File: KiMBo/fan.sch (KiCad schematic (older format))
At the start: 36 parts, among them Q14 2N7002, Q15 DMP3098L-7, Q16 2N7002, Q17 DMP3098L-7, Q18 2N7002, Q19 DMP3098L-7

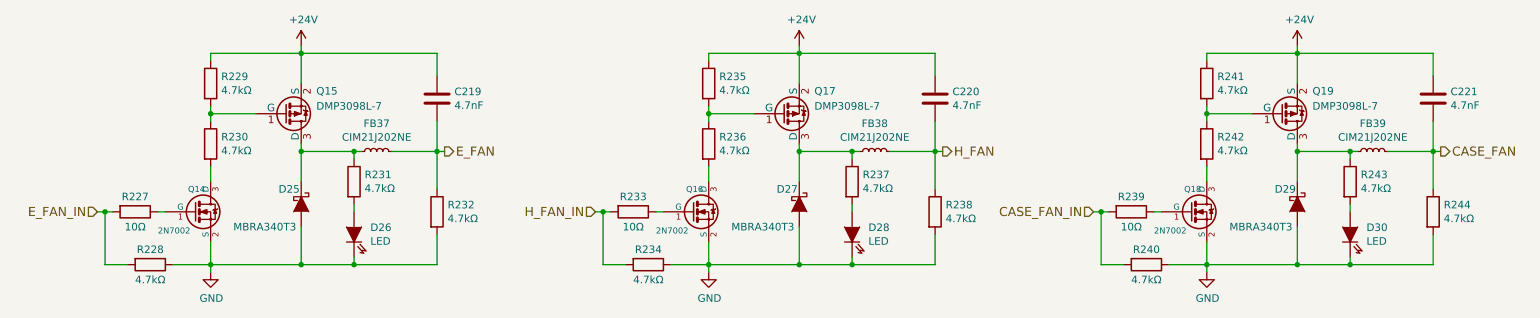
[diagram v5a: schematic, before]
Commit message: Entry of additional component values
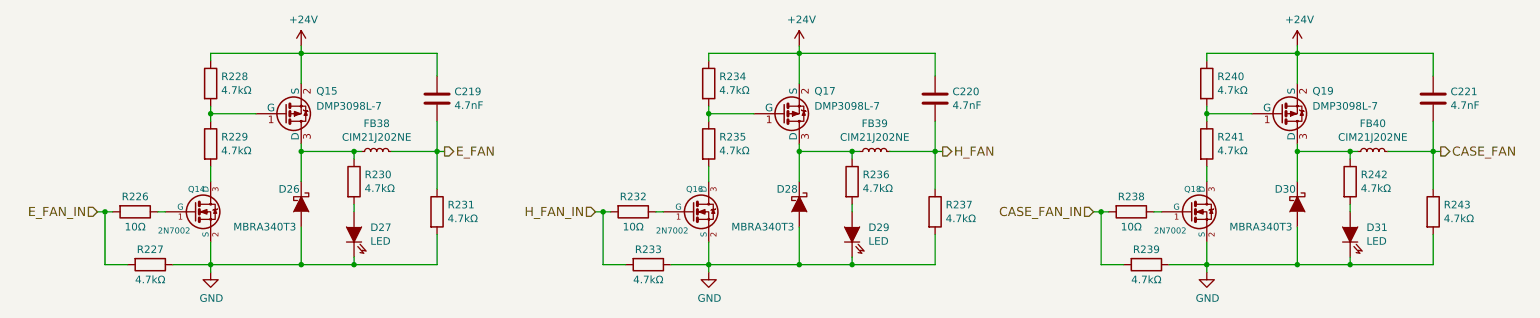
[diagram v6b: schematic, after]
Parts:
- renumbered D25 to D26, D26 to D27, D27 to D28, D28 to D29, D29 to D30, D30 to D31, FB37 to FB38, FB38 to FB39, FB39 to FB40, R227 to R226, R228 to R227, R229 to R228, R230 to R229, R231 to R230, R232 to R231, R233 to R232, R234 to R233, R235 to R234, R236 to R235, R237 to R236, R238 to R237, R239 to R238, R240 to R239, R241 to R240, R242 to R241, R243 to R242, R244 to R243
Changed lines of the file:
@@
 E_FAN
 $Comp
-L +24V #PWR0286
+L +24V #PWR0287
 U 1 1 5B5EFE55
 P 4800 4500
-F 0 "#PWR0286" H 4800 4350 50  0001 C CNN
+F 0 "#PWR0287" H 4800 4350 50  0001 C CNN
 F 1 "+24V" H 4815 4673 50  0000 C CNN
 F 2 "" H 4800 4500 50  0000 C CNN
@@
 $EndComp
 $Comp
-L GND #PWR0287
+L GND #PWR0288
 U 1 1 5B5EFE5B
 P 4200 6000
-F 0 "#PWR0287" H 4200 5750 50  0001 C CNN
+F 0 "#PWR0288" H 4200 5750 50  0001 C CNN
 F 1 "GND" H 4205 5827 50  0000 C CNN
 F 2 "" H 4200 6000 50  0000 C CNN
@@
 $EndComp
 $Comp
-L D_Schottky D25
+L D_Schottky D26
 U 1 1 5B5EFE61
 P 4800 5550
-F 0 "D25" V 4700 5400 50  0000 L CNN
+F 0 "D26" V 4700 5400 50  0000 L CNN
 F 1 "MBRA340T3" V 4950 5100 50  0000 L CNN
 F 2 "" H 4800 5550 50  0001 C CNN
@@
 $EndComp
 $Comp
-L R R227
+L R R226
 U 1 1 5B5EFE68
 P 3700 5600
-F 0 "R227" V 3600 5600 50  0000 C CNN
+F 0 "R226" V 3600 5600 50  0000 C CNN
 F 1 "10Ω" V 3800 5600 50  0000 C CNN
 F 2 "" V 3630 5600 50  0001 C CNN
@@
 $EndComp
 $Comp
-L LED_Short D26
+L LED_Short D27
 U 1 1 5B5EFE77
 P 5150 5750
-F 0 "D26" V 5196 5642 50  0000 R CNN
+F 0 "D27" V 5196 5642 50  0000 R CNN
 F 1 "LED" V 5105 5642 50  0000 R CNN
 F 2 "" H 5150 5750 50  0001 C CNN
@@
 $EndComp
 $Comp
-L R R231
+L R R230
 U 1 1 5B5EFE7E
 P 5150 5400
-F 0 "R231" H 5220 5446 50  0000 L CNN
+F 0 "R230" H 5220 5446 50  0000 L CNN
 F 1 "4.7kΩ" H 5220 5355 50  0000 L CNN
 F 2 "" V 5080 5400 50  0001 C CNN
@@
 $EndComp
 $Comp
-L R R229
+L R R228
 U 1 1 5B5EFE85
 P 4200 4750
-F 0 "R229" H 4270 4796 50  0000 L CNN
+F 0 "R228" H 4270 4796 50  0000 L CNN
 F 1 "4.7kΩ" H 4270 4705 50  0000 L CNN
 F 2 "" V 4130 4750 50  0001 C CNN
@@
 $EndComp
 $Comp
-L R R230
+L R R229
 U 1 1 5B5EFE8C
 P 4200 5150
-F 0 "R230" H 4270 5196 50  0000 L CNN
+F 0 "R229" H 4270 5196 50  0000 L CNN
 F 1 "4.7kΩ" H 4270 5105 50  0000 L CNN
 F 2 "" V 4130 5150 50  0001 C CNN
@@
 $EndComp
 $Comp
-L R R228
+L R R227
 U 1 1 5B5EFE93
 P 3800 5950
-F 0 "R228" V 3700 5950 50  0000 C CNN
+F 0 "R227" V 3700 5950 50  0000 C CNN
 F 1 "4.7kΩ" V 3900 5950 50  0000 C CNN
 F 2 "" V 3730 5950 50  0001 C CNN
@@
 $EndComp
 $Comp
-L R R232
+L R R231
 U 1 1 5B5EFE9A
 P 5700 5600
-F 0 "R232" H 5770 5646 50  0000 L CNN
+F 0 "R231" H 5770 5646 50  0000 L CNN
 F 1 "4.7kΩ" H 5770 5555 50  0000 L CNN
 F 2 "" V 5630 5600 50  0001 C CNN
@@
 $EndComp
 $Comp
-L INDUCTOR_Small FB37
+L INDUCTOR_Small FB38
 U 1 1 5B5F15E2
 P 5300 5200
-F 0 "FB37" V 5485 5200 50  0000 C CNN
+F 0 "FB38" V 5485 5200 50  0000 C CNN
 F 1 "CIM21J202NE" V 5394 5200 50  0000 C CNN
 F 2 "" H 5300 5200 50  0001 C CNN
@@
 H_FAN
 $Comp
-L +24V #PWR0288
+L +24V #PWR0289
 U 1 1 5B5F23AA
 P 8100 4500
-F 0 "#PWR0288" H 8100 4350 50  0001 C CNN
+F 0 "#PWR0289" H 8100 4350 50  0001 C CNN
 F 1 "+24V" H 8115 4673 50  0000 C CNN
 F 2 "" H 8100 4500 50  0000 C CNN
@@
 $EndComp
 $Comp
-L GND #PWR0289
+L GND #PWR0290
 U 1 1 5B5F23B0
 P 7500 6000
-F 0 "#PWR0289" H 7500 5750 50  0001 C CNN
+F 0 "#PWR0290" H 7500 5750 50  0001 C CNN
 F 1 "GND" H 7505 5827 50  0000 C CNN
 F 2 "" H 7500 6000 50  0000 C CNN
@@
 $EndComp
 $Comp
-L D_Schottky D27
+L D_Schottky D28
 U 1 1 5B5F23B6
 P 8100 5550
-F 0 "D27" V 8000 5400 50  0000 L CNN
+F 0 "D28" V 8000 5400 50  0000 L CNN
 F 1 "MBRA340T3" V 8250 5100 50  0000 L CNN
 F 2 "" H 8100 5550 50  0001 C CNN
@@
 $EndComp
 $Comp
-L R R233
+L R R232
 U 1 1 5B5F23BD
 P 7000 5600
-F 0 "R233" V 6900 5600 50  0000 C CNN
+F 0 "R232" V 6900 5600 50  0000 C CNN
 F 1 "10Ω" V 7100 5600 50  0000 C CNN
 F 2 "" V 6930 5600 50  0001 C CNN
@@
 $EndComp
 $Comp
-L LED_Short D28
+L LED_Short D29
 U 1 1 5B5F23CB
 P 8450 5750
-F 0 "D28" V 8496 5642 50  0000 R CNN
+F 0 "D29" V 8496 5642 50  0000 R CNN
 F 1 "LED" V 8405 5642 50  0000 R CNN
 F 2 "" H 8450 5750 50  0001 C CNN
@@
 $EndComp
 $Comp
-L R R237
+L R R236
 U 1 1 5B5F23D2
 P 8450 5400
-F 0 "R237" H 8520 5446 50  0000 L CNN
+F 0 "R236" H 8520 5446 50  0000 L CNN
 F 1 "4.7kΩ" H 8520 5355 50  0000 L CNN
 F 2 "" V 8380 5400 50  0001 C CNN
@@
 $EndComp
 $Comp
-L R R235
+L R R234
 U 1 1 5B5F23D9
 P 7500 4750
-F 0 "R235" H 7570 4796 50  0000 L CNN
+F 0 "R234" H 7570 4796 50  0000 L CNN
 F 1 "4.7kΩ" H 7570 4705 50  0000 L CNN
 F 2 "" V 7430 4750 50  0001 C CNN
@@
 $EndComp
 $Comp
-L R R236
+L R R235
 U 1 1 5B5F23E0
 P 7500 5150
-F 0 "R236" H 7570 5196 50  0000 L CNN
+F 0 "R235" H 7570 5196 50  0000 L CNN
 F 1 "4.7kΩ" H 7570 5105 50  0000 L CNN
 F 2 "" V 7430 5150 50  0001 C CNN
@@
 $EndComp
 $Comp
-L R R234
+L R R233
 U 1 1 5B5F23E7
 P 7100 5950
-F 0 "R234" V 7000 5950 50  0000 C CNN
+F 0 "R233" V 7000 5950 50  0000 C CNN
 F 1 "4.7kΩ" V 7200 5950 50  0000 C CNN
 F 2 "" V 7030 5950 50  0001 C CNN
@@
 $EndComp
 $Comp
-L R R238
+L R R237
 U 1 1 5B5F23EE
 P 9000 5600
-F 0 "R238" H 9070 5646 50  0000 L CNN
+F 0 "R237" H 9070 5646 50  0000 L CNN
 F 1 "4.7kΩ" H 9070 5555 50  0000 L CNN
 F 2 "" V 8930 5600 50  0001 C CNN
@@
 $EndComp
 $Comp
-L INDUCTOR_Small FB38
+L INDUCTOR_Small FB39
 U 1 1 5B5F2422
 P 8600 5200
-F 0 "FB38" V 8785 5200 50  0000 C CNN
+F 0 "FB39" V 8785 5200 50  0000 C CNN
 F 1 "CIM21J202NE" V 8694 5200 50  0000 C CNN
 F 2 "" H 8600 5200 50  0001 C CNN
@@
 CASE_FAN
 $Comp
-L +24V #PWR0290
+L +24V #PWR0291
 U 1 1 5B5F2995
 P 11400 4500
-F 0 "#PWR0290" H 11400 4350 50  0001 C CNN
+F 0 "#PWR0291" H 11400 4350 50  0001 C CNN
 F 1 "+24V" H 11415 4673 50  0000 C CNN
 F 2 "" H 11400 4500 50  0000 C CNN
@@
 $EndComp
 $Comp
-L GND #PWR0291
+L GND #PWR0292
 U 1 1 5B5F299B
 P 10800 6000
-F 0 "#PWR0291" H 10800 5750 50  0001 C CNN
+F 0 "#PWR0292" H 10800 5750 50  0001 C CNN
 F 1 "GND" H 10805 5827 50  0000 C CNN
 F 2 "" H 10800 6000 50  0000 C CNN
@@
 $EndComp
 $Comp
-L D_Schottky D29
+L D_Schottky D30
 U 1 1 5B5F29A1
 P 11400 5550
-F 0 "D29" V 11300 5400 50  0000 L CNN
+F 0 "D30" V 11300 5400 50  0000 L CNN
 F 1 "MBRA340T3" V 11550 5100 50  0000 L CNN
 F 2 "" H 11400 5550 50  0001 C CNN
@@
 $EndComp
 $Comp
-L R R239
+L R R238
 U 1 1 5B5F29A8
 P 10300 5600
-F 0 "R239" V 10200 5600 50  0000 C CNN
+F 0 "R238" V 10200 5600 50  0000 C CNN
 F 1 "10Ω" V 10400 5600 50  0000 C CNN
 F 2 "" V 10230 5600 50  0001 C CNN
@@
 $EndComp
 $Comp
-L LED_Short D30
+L LED_Short D31
 U 1 1 5B5F29B6
 P 11750 5750
-F 0 "D30" V 11796 5642 50  0000 R CNN
+F 0 "D31" V 11796 5642 50  0000 R CNN
 F 1 "LED" V 11705 5642 50  0000 R CNN
 F 2 "" H 11750 5750 50  0001 C CNN
@@
 $EndComp
 $Comp
-L R R243
+L R R242
 U 1 1 5B5F29BD
 P 11750 5400
-F 0 "R243" H 11820 5446 50  0000 L CNN
+F 0 "R242" H 11820 5446 50  0000 L CNN
 F 1 "4.7kΩ" H 11820 5355 50  0000 L CNN
 F 2 "" V 11680 5400 50  0001 C CNN
@@
 $EndComp
 $Comp
-L R R241
+L R R240
 U 1 1 5B5F29C4
 P 10800 4750
-F 0 "R241" H 10870 4796 50  0000 L CNN
+F 0 "R240" H 10870 4796 50  0000 L CNN
 F 1 "4.7kΩ" H 10870 4705 50  0000 L CNN
 F 2 "" V 10730 4750 50  0001 C CNN
@@
 $EndComp
 $Comp
-L R R242
+L R R241
 U 1 1 5B5F29CB
 P 10800 5150
-F 0 "R242" H 10870 5196 50  0000 L CNN
+F 0 "R241" H 10870 5196 50  0000 L CNN
 F 1 "4.7kΩ" H 10870 5105 50  0000 L CNN
 F 2 "" V 10730 5150 50  0001 C CNN
@@
 $EndComp
 $Comp
-L R R240
+L R R239
 U 1 1 5B5F29D2
 P 10400 5950
-F 0 "R240" V 10300 5950 50  0000 C CNN
+F 0 "R239" V 10300 5950 50  0000 C CNN
 F 1 "4.7kΩ" V 10500 5950 50  0000 C CNN
 F 2 "" V 10330 5950 50  0001 C CNN
@@
 $EndComp
 $Comp
-L R R244
+L R R243
 U 1 1 5B5F29D9
 P 12300 5600
-F 0 "R244" H 12370 5646 50  0000 L CNN
+F 0 "R243" H 12370 5646 50  0000 L CNN
 F 1 "4.7kΩ" H 12370 5555 50  0000 L CNN
 F 2 "" V 12230 5600 50  0001 C CNN
@@
 $EndComp
 $Comp
-L INDUCTOR_Small FB39
+L INDUCTOR_Small FB40
 U 1 1 5B5F2A0D
 P 11900 5200
-F 0 "FB39" V 12085 5200 50  0000 C CNN
+F 0 "FB40" V 12085 5200 50  0000 C CNN
 F 1 "CIM21J202NE" V 11994 5200 50  0000 C CNN
 F 2 "" H 11900 5200 50  0001 C CNN

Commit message: Add equivalent annotations document, associate more footprints
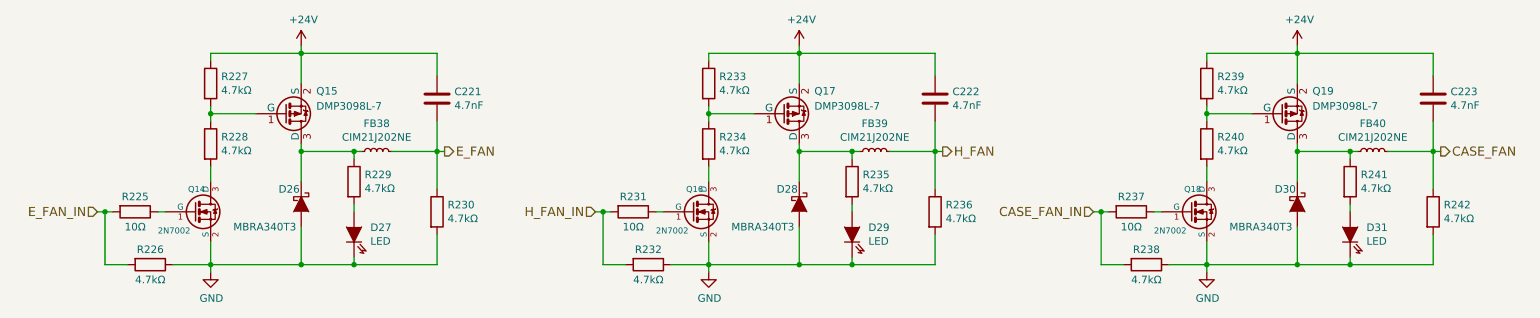
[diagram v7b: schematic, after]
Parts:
- C221: renamed from C219; footprint (none) -> Capacitors_SMD:C_0402
- C222: renamed from C220; footprint (none) -> Capacitors_SMD:C_0402
- C223: renamed from C221; footprint (none) -> Capacitors_SMD:C_0402
- renumbered R226 to R225, R227 to R226, R228 to R227, R229 to R228, R230 to R229, R231 to R230, R232 to R231, R233 to R232, R234 to R233, R235 to R234, R236 to R235, R237 to R236, R238 to R237, R239 to R238, R240 to R239, R241 to R240, R242 to R241, R243 to R242
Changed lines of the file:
@@
 E_FAN
 $Comp
-L +24V #PWR0287
+L +24V #PWR0288
 U 1 1 5B5EFE55
 P 4800 4500
-F 0 "#PWR0287" H 4800 4350 50  0001 C CNN
+F 0 "#PWR0288" H 4800 4350 50  0001 C CNN
 F 1 "+24V" H 4815 4673 50  0000 C CNN
 F 2 "" H 4800 4500 50  0000 C CNN
@@
 $EndComp
 $Comp
-L GND #PWR0288
+L GND #PWR0289
 U 1 1 5B5EFE5B
 P 4200 6000
-F 0 "#PWR0288" H 4200 5750 50  0001 C CNN
+F 0 "#PWR0289" H 4200 5750 50  0001 C CNN
 F 1 "GND" H 4205 5827 50  0000 C CNN
 F 2 "" H 4200 6000 50  0000 C CNN
@@
 $EndComp
 $Comp
-L R R226
+L R R225
 U 1 1 5B5EFE68
 P 3700 5600
-F 0 "R226" V 3600 5600 50  0000 C CNN
+F 0 "R225" V 3600 5600 50  0000 C CNN
 F 1 "10Ω" V 3800 5600 50  0000 C CNN
 F 2 "" V 3630 5600 50  0001 C CNN
@@
 $EndComp
 $Comp
-L R R230
+L R R229
 U 1 1 5B5EFE7E
 P 5150 5400
-F 0 "R230" H 5220 5446 50  0000 L CNN
+F 0 "R229" H 5220 5446 50  0000 L CNN
 F 1 "4.7kΩ" H 5220 5355 50  0000 L CNN
 F 2 "" V 5080 5400 50  0001 C CNN
@@
 $EndComp
 $Comp
-L R R228
+L R R227
 U 1 1 5B5EFE85
 P 4200 4750
-F 0 "R228" H 4270 4796 50  0000 L CNN
+F 0 "R227" H 4270 4796 50  0000 L CNN
 F 1 "4.7kΩ" H 4270 4705 50  0000 L CNN
 F 2 "" V 4130 4750 50  0001 C CNN
@@
 $EndComp
 $Comp
-L R R229
+L R R228
 U 1 1 5B5EFE8C
 P 4200 5150
-F 0 "R229" H 4270 5196 50  0000 L CNN
+F 0 "R228" H 4270 5196 50  0000 L CNN
 F 1 "4.7kΩ" H 4270 5105 50  0000 L CNN
 F 2 "" V 4130 5150 50  0001 C CNN
@@
 $EndComp
 $Comp
-L R R227
+L R R226
 U 1 1 5B5EFE93
 P 3800 5950
-F 0 "R227" V 3700 5950 50  0000 C CNN
+F 0 "R226" V 3700 5950 50  0000 C CNN
 F 1 "4.7kΩ" V 3900 5950 50  0000 C CNN
 F 2 "" V 3730 5950 50  0001 C CNN
@@
 $EndComp
 $Comp
-L R R231
+L R R230
 U 1 1 5B5EFE9A
 P 5700 5600
-F 0 "R231" H 5770 5646 50  0000 L CNN
+F 0 "R230" H 5770 5646 50  0000 L CNN
 F 1 "4.7kΩ" H 5770 5555 50  0000 L CNN
 F 2 "" V 5630 5600 50  0001 C CNN
@@
 $EndComp
 $Comp
-L C C219
+L C C221
 U 1 1 5B5EFEA1
 P 5700 4850
-F 0 "C219" H 5815 4896 50  0000 L CNN
+F 0 "C221" H 5815 4896 50  0000 L CNN
 F 1 "4.7nF" H 5815 4805 50  0000 L CNN
-F 2 "" H 5738 4700 50  0001 C CNN
+F 2 "Capacitors_SMD:C_0402" H 5738 4700 50  0001 C CNN
 F 3 "" H 5700 4850 50  0000 C CNN
 	1    5700 4850
@@
 H_FAN
 $Comp
-L +24V #PWR0289
+L +24V #PWR0290
 U 1 1 5B5F23AA
 P 8100 4500
-F 0 "#PWR0289" H 8100 4350 50  0001 C CNN
+F 0 "#PWR0290" H 8100 4350 50  0001 C CNN
 F 1 "+24V" H 8115 4673 50  0000 C CNN
 F 2 "" H 8100 4500 50  0000 C CNN
@@
 $EndComp
 $Comp
-L GND #PWR0290
+L GND #PWR0291
 U 1 1 5B5F23B0
 P 7500 6000
-F 0 "#PWR0290" H 7500 5750 50  0001 C CNN
+F 0 "#PWR0291" H 7500 5750 50  0001 C CNN
 F 1 "GND" H 7505 5827 50  0000 C CNN
 F 2 "" H 7500 6000 50  0000 C CNN
@@
 $EndComp
 $Comp
-L R R232
+L R R231
 U 1 1 5B5F23BD
 P 7000 5600
-F 0 "R232" V 6900 5600 50  0000 C CNN
+F 0 "R231" V 6900 5600 50  0000 C CNN
 F 1 "10Ω" V 7100 5600 50  0000 C CNN
 F 2 "" V 6930 5600 50  0001 C CNN
@@
 $EndComp
 $Comp
-L R R236
+L R R235
 U 1 1 5B5F23D2
 P 8450 5400
-F 0 "R236" H 8520 5446 50  0000 L CNN
+F 0 "R235" H 8520 5446 50  0000 L CNN
 F 1 "4.7kΩ" H 8520 5355 50  0000 L CNN
 F 2 "" V 8380 5400 50  0001 C CNN
@@
 $EndComp
 $Comp
-L R R234
+L R R233
 U 1 1 5B5F23D9
 P 7500 4750
-F 0 "R234" H 7570 4796 50  0000 L CNN
+F 0 "R233" H 7570 4796 50  0000 L CNN
 F 1 "4.7kΩ" H 7570 4705 50  0000 L CNN
 F 2 "" V 7430 4750 50  0001 C CNN
@@
 $EndComp
 $Comp
-L R R235
+L R R234
 U 1 1 5B5F23E0
 P 7500 5150
-F 0 "R235" H 7570 5196 50  0000 L CNN
+F 0 "R234" H 7570 5196 50  0000 L CNN
 F 1 "4.7kΩ" H 7570 5105 50  0000 L CNN
 F 2 "" V 7430 5150 50  0001 C CNN
@@
 $EndComp
 $Comp
-L R R233
+L R R232
 U 1 1 5B5F23E7
 P 7100 5950
-F 0 "R233" V 7000 5950 50  0000 C CNN
+F 0 "R232" V 7000 5950 50  0000 C CNN
 F 1 "4.7kΩ" V 7200 5950 50  0000 C CNN
 F 2 "" V 7030 5950 50  0001 C CNN
@@
 $EndComp
 $Comp
-L R R237
+L R R236
 U 1 1 5B5F23EE
 P 9000 5600
-F 0 "R237" H 9070 5646 50  0000 L CNN
+F 0 "R236" H 9070 5646 50  0000 L CNN
 F 1 "4.7kΩ" H 9070 5555 50  0000 L CNN
 F 2 "" V 8930 5600 50  0001 C CNN
@@
 $EndComp
 $Comp
-L C C220
+L C C222
 U 1 1 5B5F23F5
 P 9000 4850
-F 0 "C220" H 9115 4896 50  0000 L CNN
+F 0 "C222" H 9115 4896 50  0000 L CNN
 F 1 "4.7nF" H 9115 4805 50  0000 L CNN
-F 2 "" H 9038 4700 50  0001 C CNN
+F 2 "Capacitors_SMD:C_0402" H 9038 4700 50  0001 C CNN
 F 3 "" H 9000 4850 50  0000 C CNN
 	1    9000 4850
@@
 CASE_FAN
 $Comp
-L +24V #PWR0291
+L +24V #PWR0292
 U 1 1 5B5F2995
 P 11400 4500
-F 0 "#PWR0291" H 11400 4350 50  0001 C CNN
+F 0 "#PWR0292" H 11400 4350 50  0001 C CNN
 F 1 "+24V" H 11415 4673 50  0000 C CNN
 F 2 "" H 11400 4500 50  0000 C CNN
@@
 $EndComp
 $Comp
-L GND #PWR0292
+L GND #PWR0293
 U 1 1 5B5F299B
 P 10800 6000
-F 0 "#PWR0292" H 10800 5750 50  0001 C CNN
+F 0 "#PWR0293" H 10800 5750 50  0001 C CNN
 F 1 "GND" H 10805 5827 50  0000 C CNN
 F 2 "" H 10800 6000 50  0000 C CNN
@@
 $EndComp
 $Comp
-L R R238
+L R R237
 U 1 1 5B5F29A8
 P 10300 5600
-F 0 "R238" V 10200 5600 50  0000 C CNN
+F 0 "R237" V 10200 5600 50  0000 C CNN
 F 1 "10Ω" V 10400 5600 50  0000 C CNN
 F 2 "" V 10230 5600 50  0001 C CNN
@@
 $EndComp
 $Comp
-L R R242
+L R R241
 U 1 1 5B5F29BD
 P 11750 5400
-F 0 "R242" H 11820 5446 50  0000 L CNN
+F 0 "R241" H 11820 5446 50  0000 L CNN
 F 1 "4.7kΩ" H 11820 5355 50  0000 L CNN
 F 2 "" V 11680 5400 50  0001 C CNN
@@
 $EndComp
 $Comp
-L R R240
+L R R239
 U 1 1 5B5F29C4
 P 10800 4750
-F 0 "R240" H 10870 4796 50  0000 L CNN
+F 0 "R239" H 10870 4796 50  0000 L CNN
 F 1 "4.7kΩ" H 10870 4705 50  0000 L CNN
 F 2 "" V 10730 4750 50  0001 C CNN
@@
 $EndComp
 $Comp
-L R R241
+L R R240
 U 1 1 5B5F29CB
 P 10800 5150
-F 0 "R241" H 10870 5196 50  0000 L CNN
+F 0 "R240" H 10870 5196 50  0000 L CNN
 F 1 "4.7kΩ" H 10870 5105 50  0000 L CNN
 F 2 "" V 10730 5150 50  0001 C CNN
@@
 $EndComp
 $Comp
-L R R239
+L R R238
 U 1 1 5B5F29D2
 P 10400 5950
-F 0 "R239" V 10300 5950 50  0000 C CNN
+F 0 "R238" V 10300 5950 50  0000 C CNN
 F 1 "4.7kΩ" V 10500 5950 50  0000 C CNN
 F 2 "" V 10330 5950 50  0001 C CNN
@@
 $EndComp
 $Comp
-L R R243
+L R R242
 U 1 1 5B5F29D9
 P 12300 5600
-F 0 "R243" H 12370 5646 50  0000 L CNN
+F 0 "R242" H 12370 5646 50  0000 L CNN
 F 1 "4.7kΩ" H 12370 5555 50  0000 L CNN
 F 2 "" V 12230 5600 50  0001 C CNN
@@
 $EndComp
 $Comp
-L C C221
+L C C223
 U 1 1 5B5F29E0
 P 12300 4850
-F 0 "C221" H 12415 4896 50  0000 L CNN
+F 0 "C223" H 12415 4896 50  0000 L CNN
 F 1 "4.7nF" H 12415 4805 50  0000 L CNN
-F 2 "" H 12338 4700 50  0001 C CNN
+F 2 "Capacitors_SMD:C_0402" H 12338 4700 50  0001 C CNN
 F 3 "" H 12300 4850 50  0000 C CNN
 	1    12300 4850
